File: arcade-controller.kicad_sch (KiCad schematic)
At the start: 10 parts, among them J1 Conn_01x05_Pin, SW1 SW_Push, SW2 SW_Push, SW3 SW_Push, SW4 SW_Push, SW5 SW_Push, SW6 SW_Push, SW7 SW_Push, SW8 SW_Push

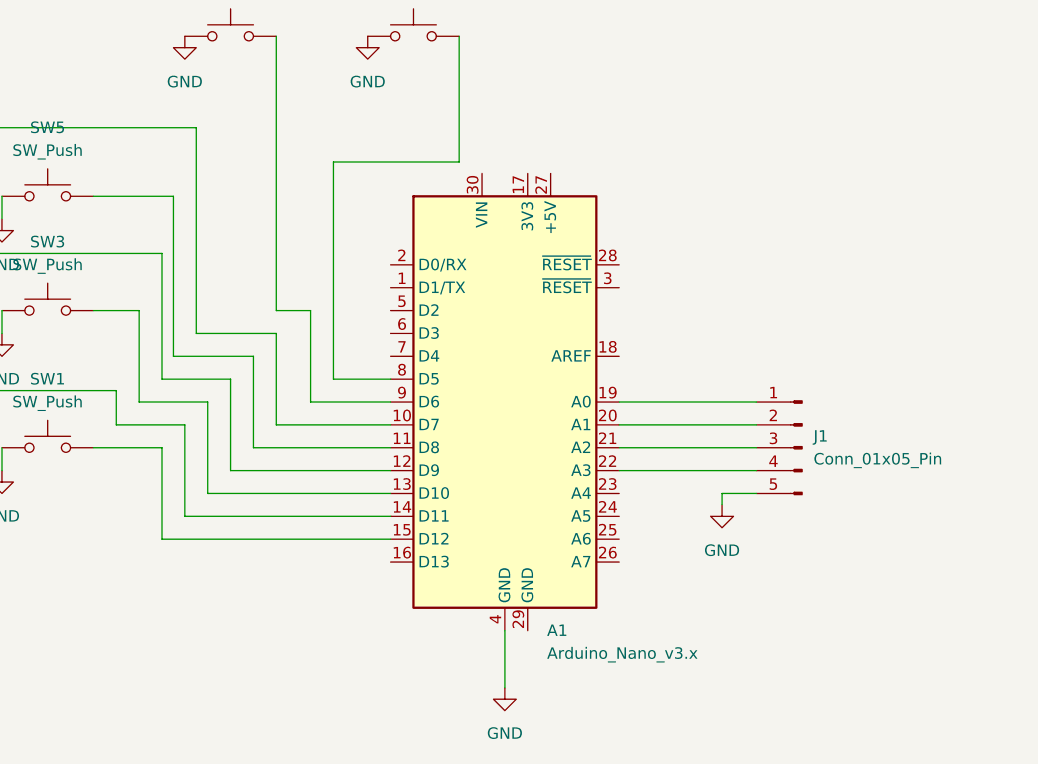
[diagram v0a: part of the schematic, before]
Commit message: Fixed it with proMicro
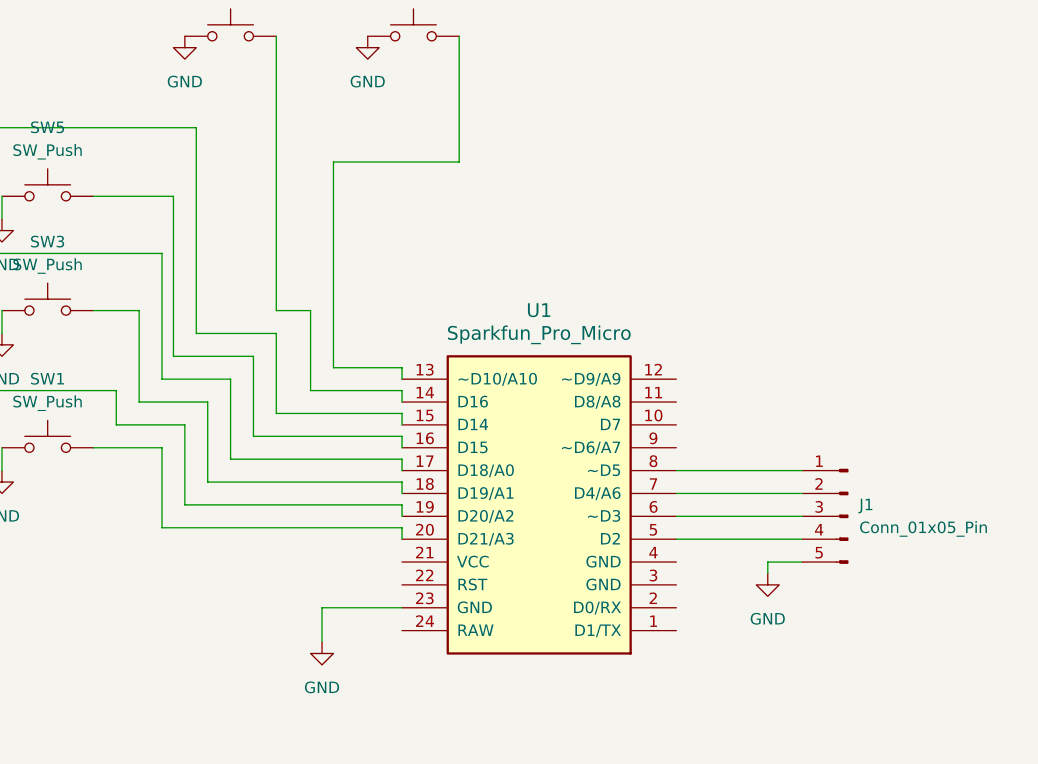
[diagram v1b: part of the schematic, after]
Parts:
- removed A1: Arduino_Nano_v3.x, Module:Arduino_Nano, symbol MCU_Module:Arduino_Nano_v3.x
- added U1: Sparkfun_Pro_Micro, ArcadeController:Sparkfun_Pro_Micro, symbol sparkfun_pro_micro:Sparkfun_Pro_Micro
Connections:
- net GND: now also U1.23 (GND)
- net at J1.1 (Pin_1): now also U1.8 (~D5)
- net at J1.2 (Pin_2): now also U1.7 (D4/A6)
- net at J1.3 (Pin_3): now also U1.6 (~D3)
- net at J1.4 (Pin_4): now also U1.5 (D2)
- net at SW4.2: now also U1.17 (D18/A0)
- net at SW7.2: now also U1.14 (D16)
- net at SW2.2: now also U1.19 (D20/A2)
- net at SW6.2: now also U1.15 (D14)
- net at SW5.2: now also U1.16 (D15)
- net at SW3.2: now also U1.18 (D19/A1)
- net at SW1.2: now also U1.20 (D21/A3)
- net at SW8.2: now also U1.13 (~D10/A10)
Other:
- moved on the sheet: J1

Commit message: added mounting holes
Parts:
- added H1, H2, H3, H4: MountingHole, MountingHole:MountingHole_3.2mm_M3, symbol Mechanical:MountingHole
